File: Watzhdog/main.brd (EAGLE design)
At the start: 100 x 80 mm, 44 parts, among them CN1 MICROUSB(MC-5F-02), IC1 C8051F381-GM, IC3 N25Q512A, IC6 MPU-9250, U1 MCP73831, U2 TPS61201

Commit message: 回路図修正完了 モジュールごとに見やすくした DCDC の高周波ラインを分離 各所パスコン追加 EEPROM のCS ラインにプルアップ追加
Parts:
- added C12, C14: 0.1u, reg,cap:1005
- added C13, C4: 22uF, CH_passive:0805
- added R6: 100k, reg,cap:1005
- R26: value 1k -> 100k
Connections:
- net N$5 renamed PWR_EN_1
- net N$6 renamed PWR_EN
- net N$7 renamed PWR_EN_2
- removed net VBAT: C2.1, JP1.2, L1.P$2, R2.2, S1.1, S1.2, U1.3, U2.5
- removed net VCC: C1.1, C10.P$2, C11.P$2, C6.1, C7.P$2, C9.P$2, IC1.6, IC1.7, IC3.3, IC3.7, IC3.8, IC6.1, IC6.13, IC6.8, MP.TP, R11.P$2, U2.10, U2.2
- new net +3V3: C1.1, C10.P$2, C11.P$2, C13.1, C14.P$2, C6.1, C7.P$2, C9.P$2, IC1.6, IC1.7, IC3.3, IC3.7, IC3.8, IC6.1, IC6.13, IC6.8, MP.TP, R11.P$2, R6.P$2, U2.10, U2.2
- new net PGND: C1.2, C12.P$1, C13.2, C4.2, U2.11, U2.12, U2.13, U2.14, U2.15, U2.4
- new net VDD_BATT: C12.P$2, C2.1, C4.1, JP1.2, L1.P$2, R2.2, S1.1, S1.2, U1.3, U2.5
- net DGND: now also C14.P$1; no longer C1.2, U2.11, U2.12, U2.13, U2.14, U2.15, U2.4
- net EEPROM_!CS: now also R6.P$1
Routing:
- net VCC: track 86.2 -> 0.00 mm, vias 6 -> 0
- net +3V3: track 0.00 -> 81.3 mm, vias 0 -> 6
- net VBAT: track 60.3 -> 0.00 mm, vias 3 -> 0
- net VDD_BATT: track 0.00 -> 58.3 mm, vias 0 -> 3
- net DGND: track 56.9 -> 52.3 mm, vias 5 -> 4
- net D+: track 31.8 -> 28.6 mm
- net PWR_EN_1: track 6.18 -> 3.57 mm
- net D-: track 31.5 -> 29.3 mm
- net PGND: track 0.00 -> 2.23 mm
- net PWR_EN: track 35.4 -> 33.9 mm
- net PWR_EN_2: track 11.0 -> 10.4 mm
- net VBUS: track 33.6 -> 33.0 mm
- net STAT: track 2.93 -> 2.43 mm

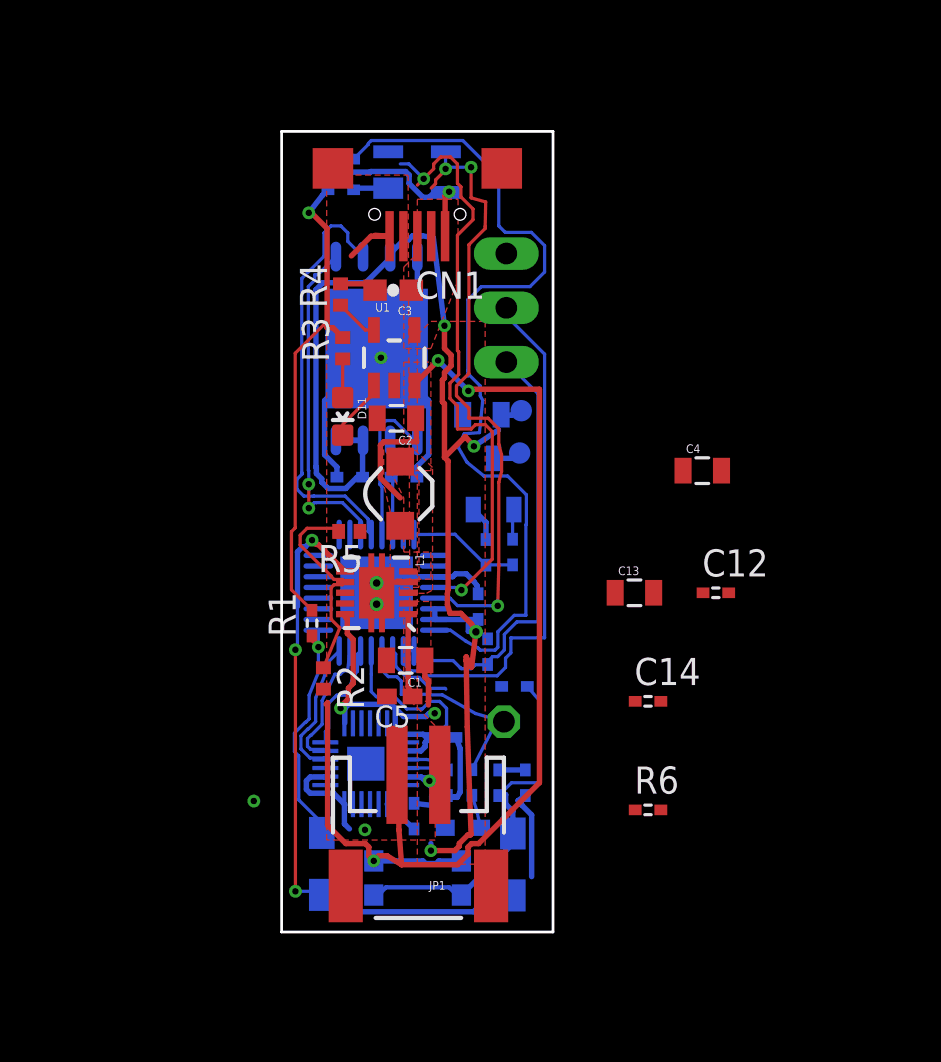
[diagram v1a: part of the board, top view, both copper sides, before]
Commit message: 部品配置の再検討中 SW電源，充電IC，USB インターフェース周りは完了 残：モータFET，マイコン，周辺IC
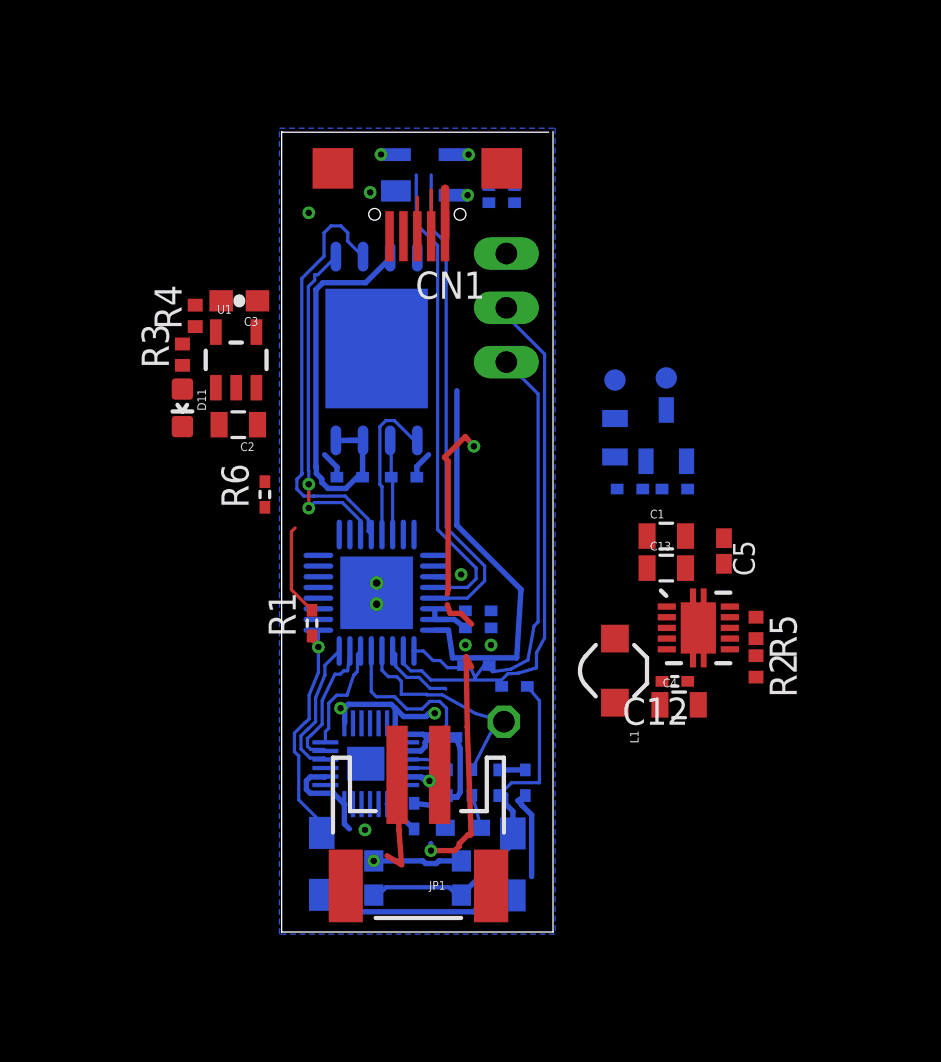
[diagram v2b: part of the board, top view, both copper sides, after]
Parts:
- moved R6 23.2 mm to (50.0, 47.1), turned to 90 degrees
- moved R2 20.3 mm to (73.0, 39.1)
- moved R5 19.6 mm to (73.0, 40.9), turned to 270 degrees
- moved C5 16.6 mm to (71.5, 44.5), turned to 270 degrees
- moved U2 15.1 mm to (70.3, 40.9), turned to 270 degrees
- moved C1 13.5 mm to (68.8, 45.2), turned to 0 degrees
- moved L1 13.0 mm to (66.4, 38.9)
- moved C4 11.0 mm to (69.4, 37.3)
- moved C14 9.00 mm to (60.0, 41.7), flipped to the bottom
- moved FET1 8.39 mm to (68.8, 49.9)
- moved R17 8.15 mm to (69.2, 47.4), turned to 0 degrees
- moved R10 7.80 mm to (61.1, 60.8)
- moved MN 7.71 mm to (68.8, 52.6)
- moved R12 7.53 mm to (61.1, 61.6)
- moved D11 7.51 mm to (46.2, 51.2)
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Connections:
- net DGND renamed DGND2
- net N$1 renamed VAUX
- net N$2 renamed LIN
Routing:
- net VDD_BATT: track 58.3 -> 9.25 mm, vias 3 -> 1
- net DGND2: track 52.3 -> 21.7 mm, vias 4 -> 6
- net VBUS: track 33.0 -> 6.67 mm
- net +3V3: track 81.3 -> 55.3 mm, vias 6 -> 5
- net N$18: track 41.7 -> 18.7 mm
- net PWR_EN: track 33.9 -> 13.8 mm, vias 3 -> 0
- net UVLO: track 10.1 -> 0.00 mm
- net PWM: track 5.26 -> 0.00 mm
- net D+: track 28.6 -> 24.0 mm, vias 2 -> 1
- net D-: track 29.3 -> 24.9 mm, vias 3 -> 1
- net VAUX: track 3.90 -> 0.00 mm
- net STAT: track 2.43 -> 0.00 mm
- net PGND: track 2.23 -> 0.00 mm
- net PROG: track 2.04 -> 0.00 mm
- net N$3: track 1.81 -> 0.00 mm
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- removed copper zone on layer 1, net DGND2
- removed copper zone on layer 1, net LIN
- removed copper zone on layer 1, net VBAT
- removed copper zone on layer 1, net VBUS
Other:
- outline, holes or cut-outs redrawn

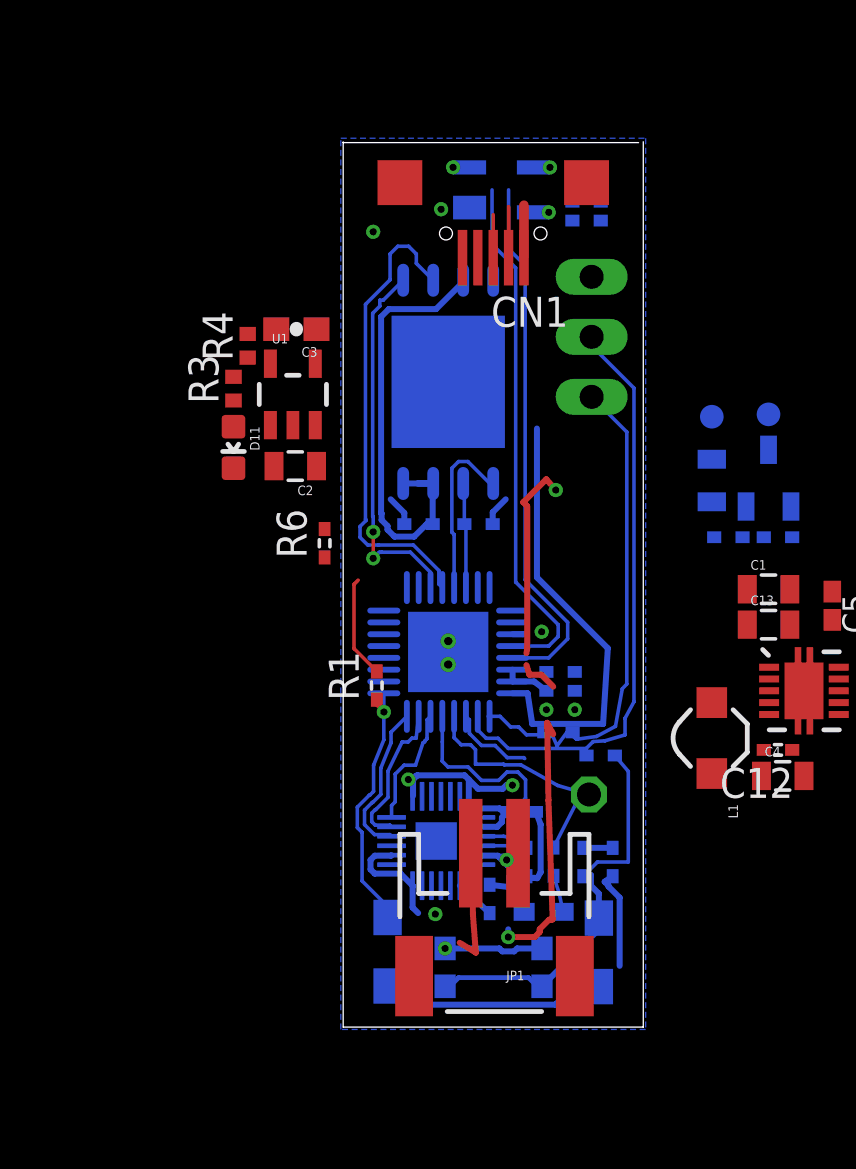
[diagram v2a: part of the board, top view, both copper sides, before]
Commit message: USBコネクタの角度を変更 ピンヘッダの大きさを再検討
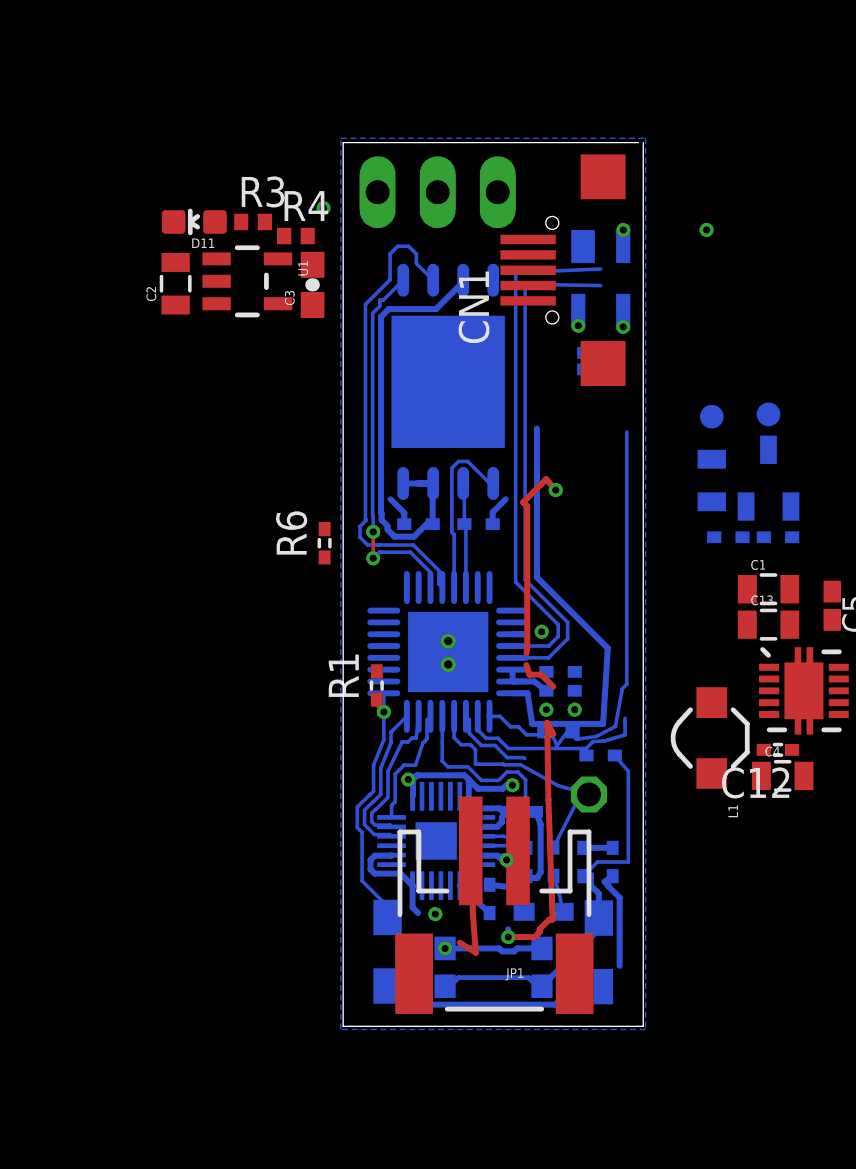
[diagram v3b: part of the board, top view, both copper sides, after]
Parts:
- moved D11 9.69 mm to (44.5, 60.7), turned to 90 degrees
- moved C2 9.23 mm to (43.7, 58.1), turned to 90 degrees
- moved JP3 8.94 mm to (54.8, 62.0), turned to 180 degrees
- moved R3 7.10 mm to (47.0, 60.7), turned to 0 degrees
- moved R12 6.42 mm to (61.6, 55.2)
- moved R10 6.32 mm to (61.6, 54.5)
- moved D3 5.63 mm to (61.7, 58.4), turned to 180 degrees
- moved U1 5.16 mm to (46.7, 58.2), turned to 270 degrees
- moved R4 5.07 mm to (48.8, 60.1), turned to 0 degrees
- moved C3 2.00 mm to (49.5, 58.1), turned to 90 degrees
- moved CN1 1.35 mm to (58.5, 58.7), turned to 90 degrees
- moved JP1 0.10 mm to (57.2, 30.4)
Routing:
- net C2D: track 25.0 -> 7.99 mm
- net VBUS: track 6.67 -> 0.12 mm
- net D-: track 24.9 -> 21.6 mm
- net D+: track 24.0 -> 21.8 mm
- net C2CK: track 21.4 -> 19.3 mm

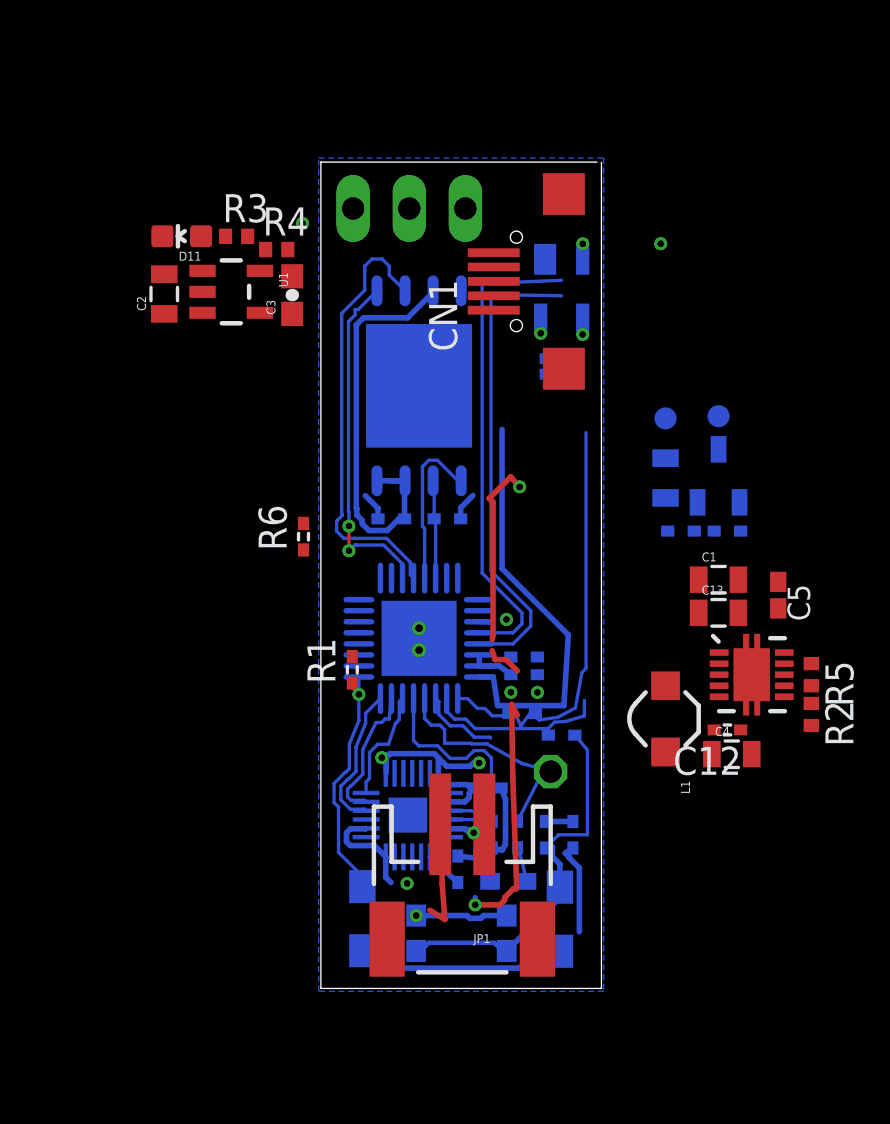
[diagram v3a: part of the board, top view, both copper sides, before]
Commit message: ピンヘッダのサイズで部品配置を決定する
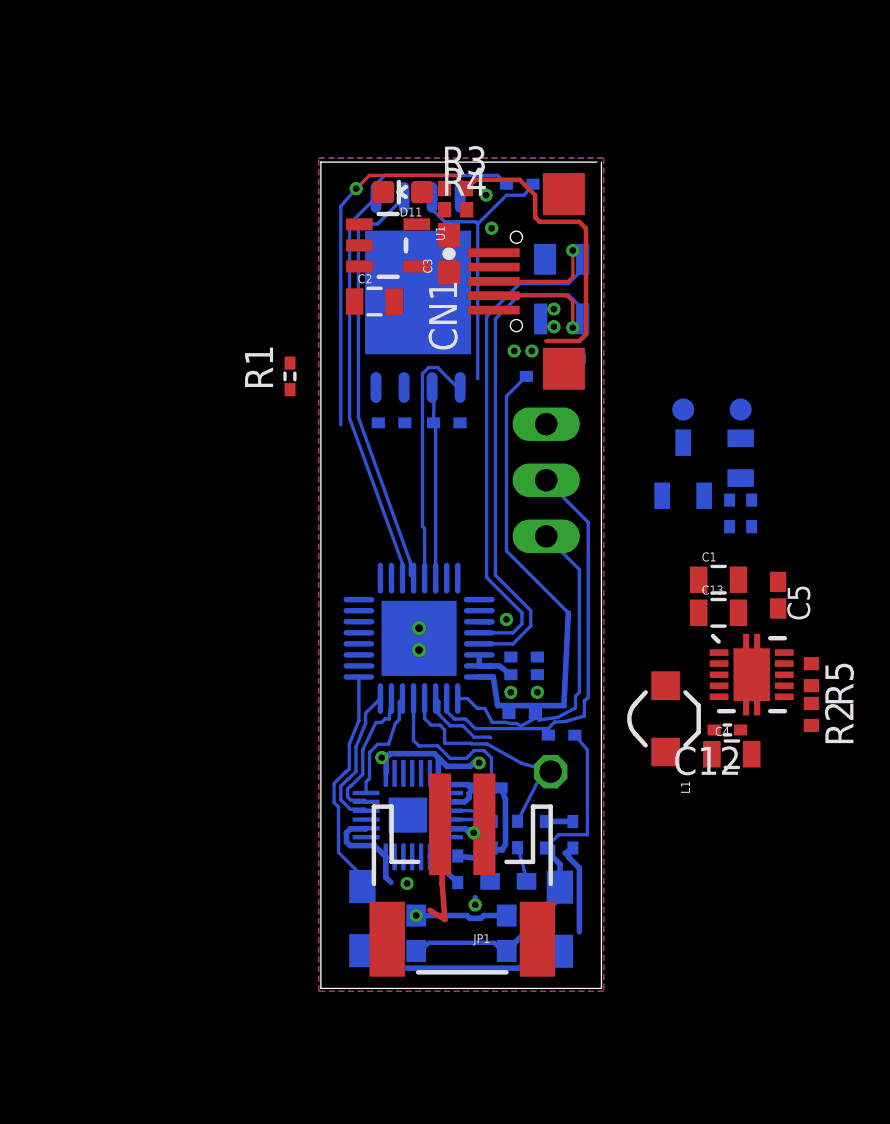
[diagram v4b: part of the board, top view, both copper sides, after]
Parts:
- moved R6 18.7 mm to (59.8, 63.1), flipped to the bottom, turned to 180 degrees
- moved JP3 13.8 mm to (61.0, 49.7), turned to 270 degrees
- moved R1 13.6 mm to (49.4, 54.4)
- moved D11 10.2 mm to (54.5, 62.7)
- moved R3 10.1 mm to (56.9, 62.9)
- moved C2 9.52 mm to (53.2, 57.8), turned to 0 degrees
- moved R4 8.30 mm to (56.9, 61.9)
- moved U1 7.40 mm to (53.8, 60.3)
- moved C3 7.34 mm to (56.6, 60.0)
- moved R26 4.34 mm to (56.5, 52.3)
- moved C11 4.34 mm to (54.0, 52.3), turned to 0 degrees
- moved IC3 4.23 mm to (55.2, 58.2)
- moved C6 3.52 mm to (69.8, 50.7)
- moved MP 3.42 mm to (69.8, 52.9)
- moved R15 3.30 mm to (70.3, 48.2), turned to 270 degrees
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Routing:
- net VBUS: track 0.12 -> 30.4 mm, vias 2 -> 5
- net +3V3: track 55.3 -> 27.7 mm, vias 5 -> 4
- net C2D: track 7.99 -> 18.9 mm
- net EEPROM_!CS: track 16.2 -> 25.0 mm, vias 2 -> 0
- net D-: track 21.6 -> 27.2 mm
- net D+: track 21.8 -> 27.2 mm
- net C2CK: track 19.3 -> 14.9 mm
- net EEPROM_SCK: track 4.45 -> 8.70 mm
- net EEPROM_MOSI: track 7.34 -> 11.5 mm
- net DGND2: track 21.7 -> 18.7 mm, vias 6 -> 7
- net N$18: track 18.7 -> 21.4 mm
- net EEPROM_MISO: track 20.0 -> 18.9 mm
- net PWR_EN_2: track 10.4 -> 9.93 mm, vias 1 -> 0
- added copper zone on layer 1, net DGND2
